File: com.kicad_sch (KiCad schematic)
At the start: 4 parts

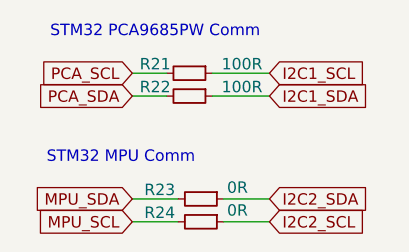
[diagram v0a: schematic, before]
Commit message: yerleştirme tamamlandı
3d modeller eklenecek
drc kontrolü yapılacak
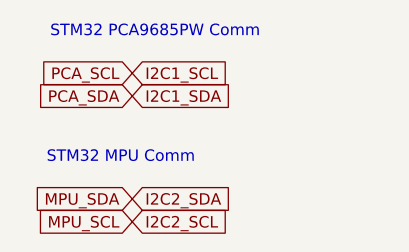
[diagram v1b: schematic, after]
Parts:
- removed R21, R22: 100R, Resistor_SMD:R_0805_2012Metric, symbol Device:R_Small
- removed R23, R24: 0R, Resistor_SMD:R_0805_2012Metric, symbol Device:R_Small
